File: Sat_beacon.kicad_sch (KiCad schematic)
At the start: 54 parts, among them IC1 LMX2581ESQE_NOPB, J1 Conn_01x03_Pin, J2 Conn_01x05_Pin, Q1 BC817, SW1 SW_Omron_B3FS, U1 STM32C011F6Px, U2 LD1117V33, U3 MCP1700x-330xxMB, Y1 FT2MHUPM10.0-T1

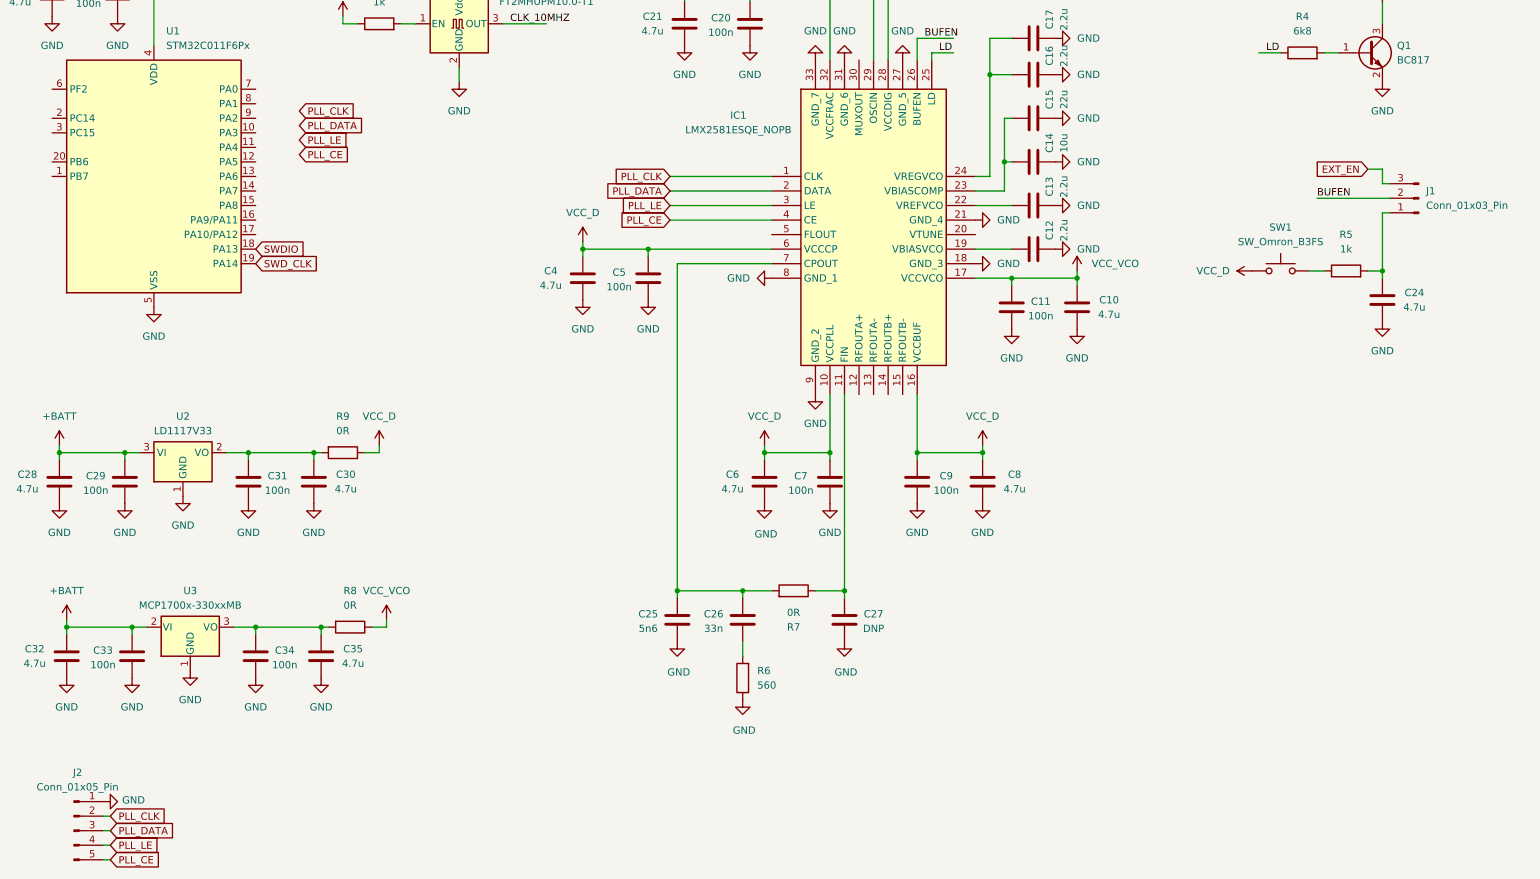
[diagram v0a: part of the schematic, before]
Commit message: added pin headers + signal nets fixes
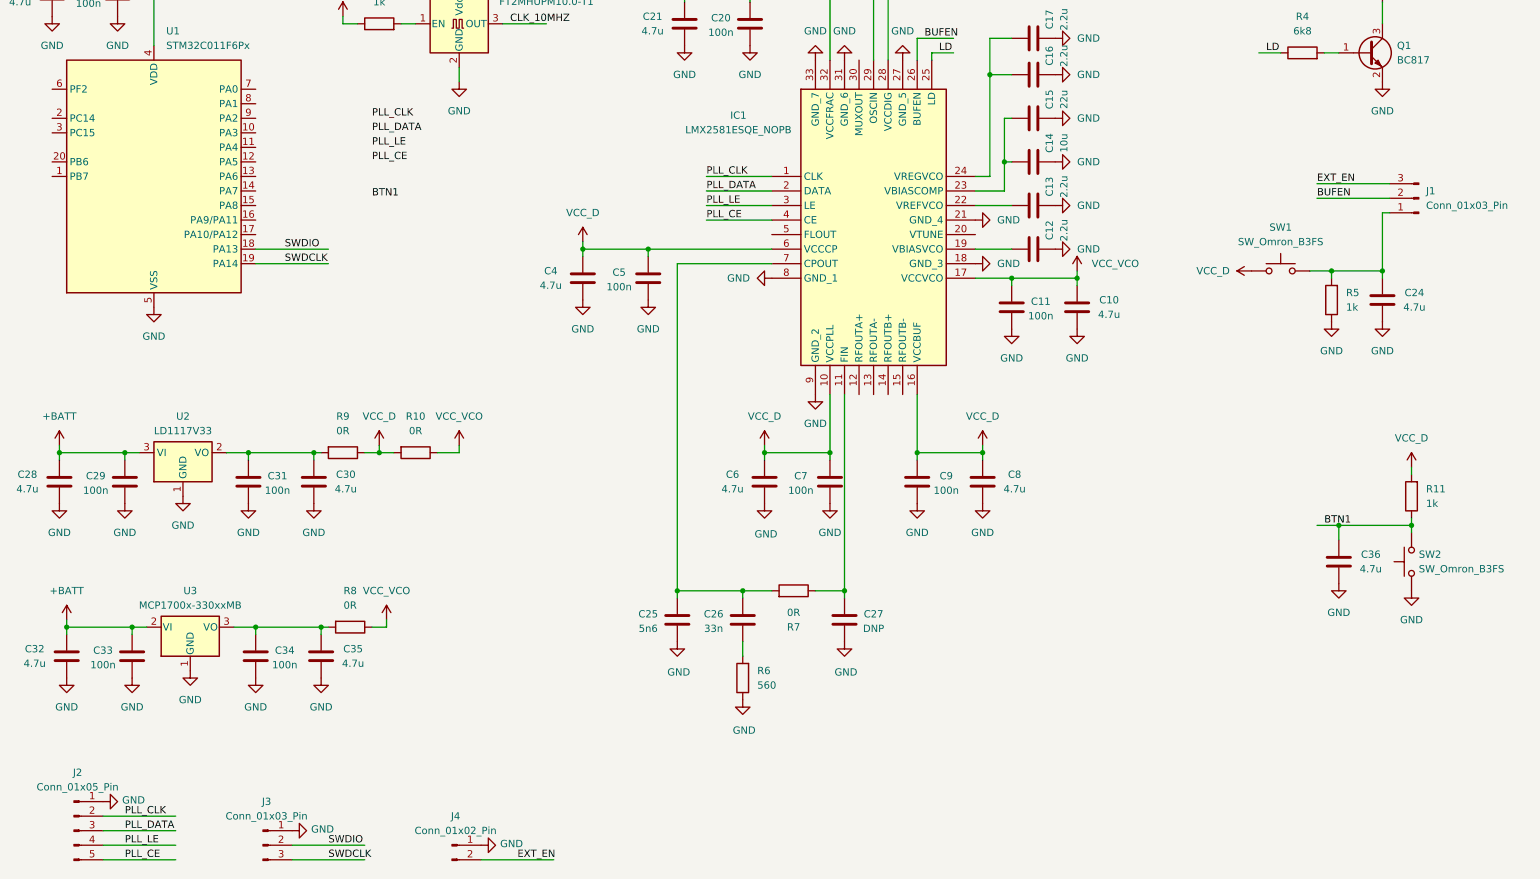
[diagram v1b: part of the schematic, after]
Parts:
- added C36: 4.7u, Capacitor_SMD:C_0805_2012Metric, symbol Device:C
- added J3: Conn_01x03_Pin, Connector_PinHeader_2.54mm:PinHeader_1x03_P2.54mm_Vertical, symbol Connector:Conn_01x03_Pin
- added J4: Conn_01x02_Pin, Connector_PinHeader_2.54mm:PinHeader_1x02_P2.54mm_Vertical, symbol Connector:Conn_01x02_Pin
- added R10: 0R, Resistor_SMD:R_0603_1608Metric, symbol Device:R
- added R11: 1k, Resistor_SMD:R_0603_1608Metric, symbol Device:R
- added SW2: SW_Omron_B3FS, Button_Switch_SMD:SW_SPST_Omron_B3FS-105xP, symbol Switch:SW_Omron_B3FS
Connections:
- net EXT_EN: now also J4.2 (Pin_2)
- net GND: now also R5.1, C36.1, J3.1 (Pin_1), J4.1 (Pin_1), SW2.1
- net SWDIO: now also J3.2 (Pin_2)
- net VCC_D: now also R10.2, R11.2
- net VCC_VCO: now also R10.1
- net at C24.2, J1.1 (Pin_1), R5.2: now also SW1.2
- net SWD_CLK renamed SWDCLK
- net SWDCLK: now also J3.3 (Pin_3)
- new net BTN1: C36.2, R11.1, SW2.2
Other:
- moved on the sheet: R5

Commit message: MCU-to-PLL pins added. Software folder created
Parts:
- added C37, C38, C39: 4.7u, Capacitor_SMD:C_0805_2012Metric, symbol Device:C
- added D2, D3: LED, LED_SMD:LED_0805_2012Metric, symbol Device:LED
- added Q2, Q3: BC817, Package_TO_SOT_SMD:SOT-23, symbol Transistor_BJT:BC817
- added R12, R13, R14: 1k, Resistor_SMD:R_0603_1608Metric, symbol Device:R
- added R15, R17: 330, Resistor_SMD:R_1206_3216Metric, symbol Device:R
- added R16, R18: 6k8, Resistor_SMD:R_0805_2012Metric, symbol Device:R
- added SW3, SW4, SW5: SW_Omron_B3FS, Button_Switch_SMD:SW_SPST_Omron_B3FS-105xP, symbol Switch:SW_Omron_B3FS
- D1: footprint LED_SMD:LED_1210_3225Metric -> LED_SMD:LED_0805_2012Metric
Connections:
- net GND: now also C37.1, C38.1, C39.1, Q2.2 (E), Q3.2 (E), SW3.1, SW4.1, SW5.1
- net PLL_CE: no longer IC1.4 (CE)
- net PLL_CLK: no longer IC1.1 (CLK)
- net PLL_DATA: no longer IC1.2 (DATA)
- net PLL_LE: no longer IC1.3 (LE)
- net VCC_D: now also D2.2 (A), D3.2 (A), R12.2, R13.2, R14.2
- net PLL_CE_1: now reaches U1.1 (PB7)
- net PLL_CE_1: now also IC1.4 (CE), U1.9 (PA2)
- net PLL_LED_1: now reaches U1.10 (PA3)
- net PLL_LED_2: now reaches U1.11 (PA4)
- net PLL_LED_2: now also R18.1
- net PLL_CE_2: now reaches U1.12 (PA5)
- net PLL_LE_2: now reaches U1.13 (PA6)
- net PLL_DATA_2: now reaches U1.14 (PA7)
- net PLL_CLK_2: now reaches U1.15 (PA8)
- net PLL_LE_1: now reaches U1.2 (PC14)
- net PLL_LE_1: now also IC1.3 (LE), U1.8 (PA1)
- net PLL_TOGGLE_2: now reaches U1.20 (PB6)
- net PLL_TOGGLE_2: now also C39.2, R14.1, SW5.2
- net PLL_DATA_1: now reaches U1.3 (PC15)
- net PLL_DATA_1: now also IC1.2 (DATA), U1.7 (PA0)
- net PLL_CLK_1: now reaches U1.6 (PF2)
- net PLL_CLK_1: now also IC1.1 (CLK)
- net BTN1 renamed PLL_BTN_1
- new net: D2.1 (K), R15.1
- new net: Q2.1 (B), R16.2
- new net: D3.1 (K), R17.1
- new net: Q3.3 (C), R17.2
- new net: Q3.1 (B), R18.2
- new net: Q2.3 (C), R15.2
- new net PLL_BTN_2: C37.2, R12.1, SW3.2
- new net PLL_TOGGLE_1: C38.2, R13.1, SW4.2
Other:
- moved on the sheet: C22, C23, C36, D1, Q1, R11, R3, R4, SW2, U1

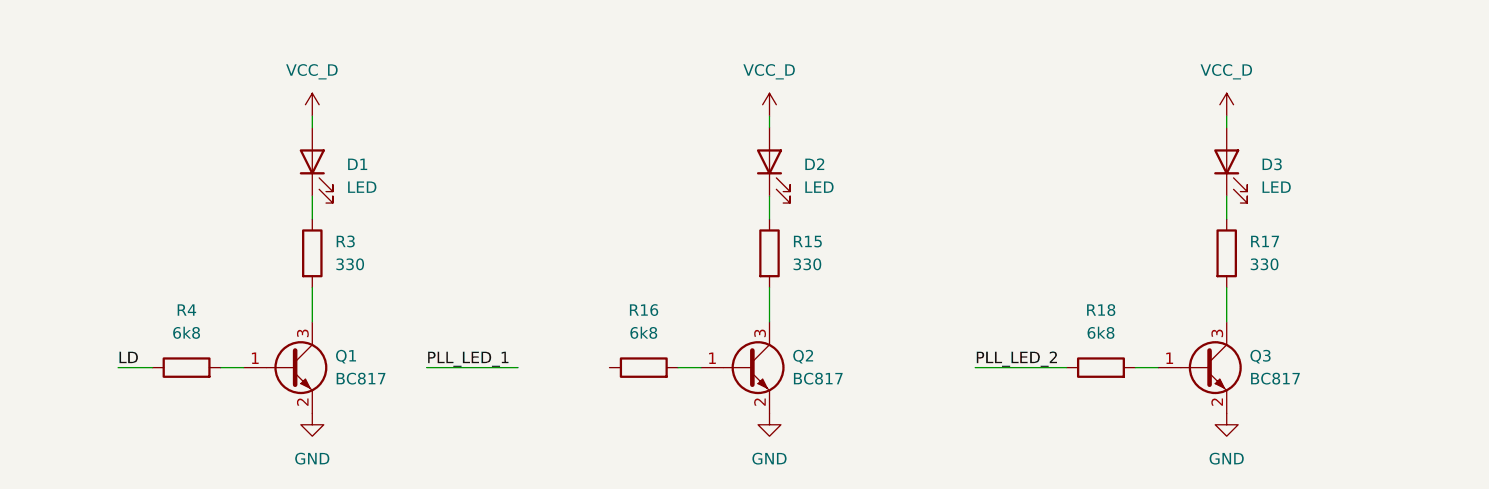
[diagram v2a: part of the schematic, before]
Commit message: picked LEDs and fixed resistors
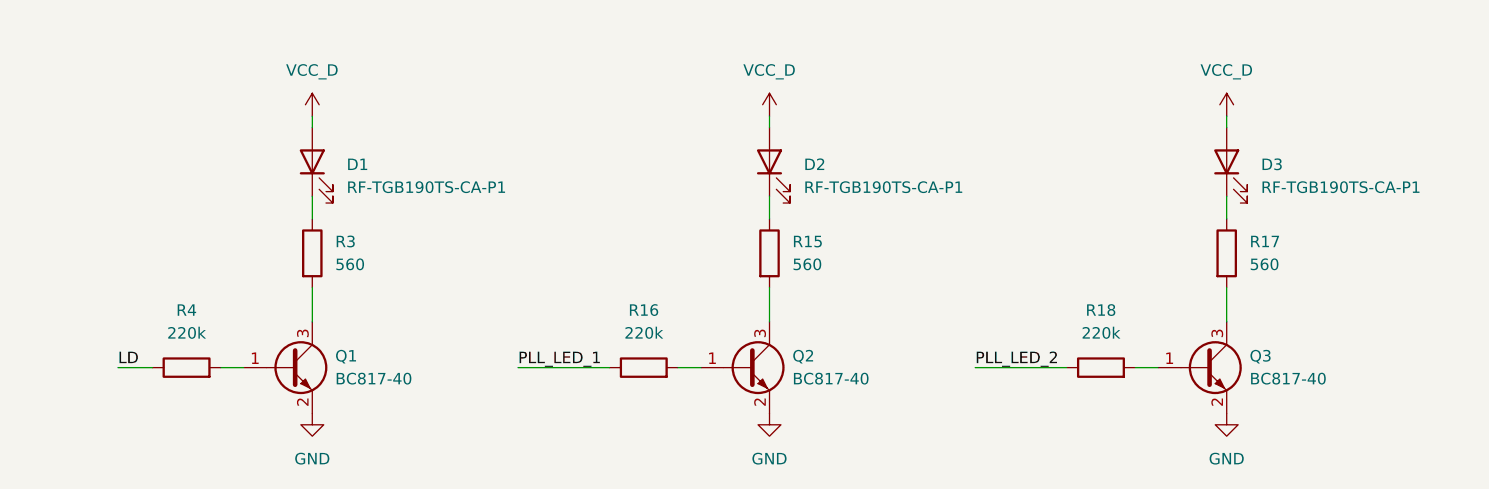
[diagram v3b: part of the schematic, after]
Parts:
- D1, D2, D3: value LED -> RF-TGB190TS-CA-P1; footprint LED_SMD:LED_0805_2012Metric -> LED_SMD:LED_0603_1608Metric
- Q1, Q2, Q3: value BC817 -> BC817-40
- R15, R17, R3: value 330 -> 560
- R16, R18, R4: value 6k8 -> 220k
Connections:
- net PLL_LED_1: now also R16.1
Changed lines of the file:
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@@
 	(wire
 		(pts
-			(xy 295.91 195.58) (xy 306.07 195.58)
+			(xy 306.07 195.58) (xy 316.23 195.58)
 		)
 		(stroke
@@
 	)
 	(label "PLL_LED_1"
-		(at 295.91 195.58 0)
+		(at 306.07 195.58 0)
 		(effects
 			(font
@@
 			)
 		)
-		(property "Value" "330"
+		(property "Value" "560"
 			(at 285.75 184.1499 0)
 			(effects
@@
 			)
 		)
-		(property "Value" "6k8"
+		(property "Value" "220k"
 			(at 269.24 191.77 90)
 			(effects
@@
 			)
 		)
-		(property "Value" "LED"
+		(property "Value" "RF-TGB190TS-CA-P1"
 			(at 337.82 175.5774 90)
 			(effects
@@
 			)
 		)
-		(property "Footprint" "LED_SMD:LED_0805_2012Metric"
+		(property "Footprint" "LED_SMD:LED_0603_1608Metric"
 			(at 334.01 172.72 0)
 			(effects
@@
 			)
 		)
-		(property "Value" "6k8"
+		(property "Value" "220k"
 			(at 320.04 191.77 90)
 			(effects
@@
 			)
 		)
-		(property "Value" "330"
+		(property "Value" "560"
 			(at 387.35 184.1499 0)
 			(effects
@@
 			)
 		)
-		(property "Value" "6k8"
+		(property "Value" "220k"
 			(at 370.84 191.77 90)
 			(effects
@@
 			)
 		)
-		(property "Value" "BC817"
+		(property "Value" "BC817-40"
 			(at 336.55 196.8499 0)
 			(effects
@@
 			)
 		)
-		(property "Value" "LED"
+		(property "Value" "RF-TGB190TS-CA-P1"
 			(at 287.02 175.5774 90)
 			(effects
@@
 			)
 		)
-		(property "Footprint" "LED_SMD:LED_0805_2012Metric"
+		(property "Footprint" "LED_SMD:LED_0603_1608Metric"
 			(at 283.21 172.72 0)
 			(effects
@@
 			)
 		)
-		(property "Value" "BC817"
+		(property "Value" "BC817-40"
 			(at 285.75 196.8499 0)
 			(effects
@@
 			)
 		)
-		(property "Value" "BC817"
+		(property "Value" "BC817-40"
 			(at 387.35 196.8499 0)
 			(effects
@@
 			)
 		)
-		(property "Value" "330"
+		(property "Value" "560"
 			(at 336.55 184.1499 0)
 			(effects
@@
 			)
 		)
-		(property "Value" "LED"
+		(property "Value" "RF-TGB190TS-CA-P1"
 			(at 388.62 175.5774 90)
 			(effects
@@
 			)
 		)
-		(property "Footprint" "LED_SMD:LED_0805_2012Metric"
+		(property "Footprint" "LED_SMD:LED_0603_1608Metric"
 			(at 384.81 172.72 0)
 			(effects

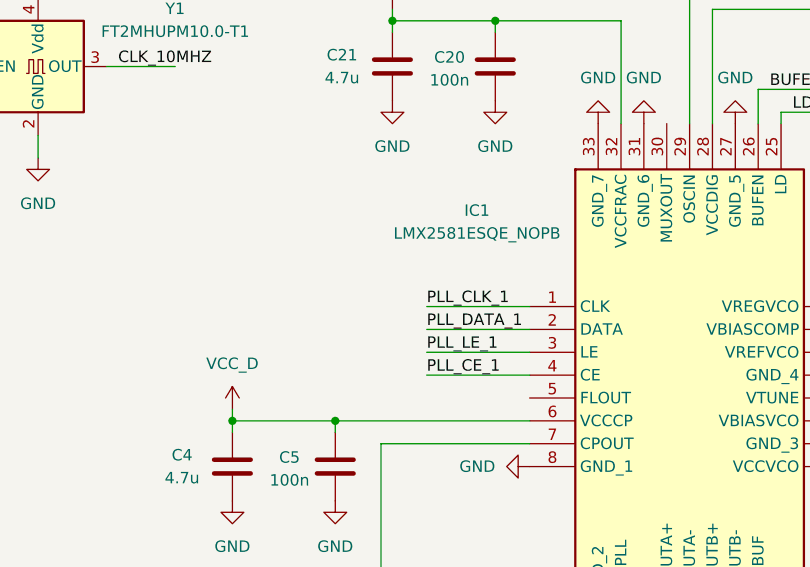
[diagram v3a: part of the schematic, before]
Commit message: PLL_LE pullup added
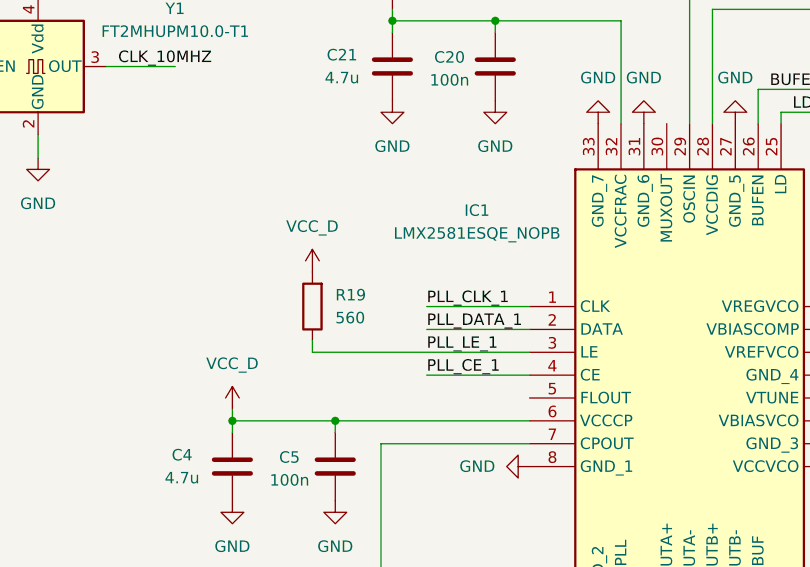
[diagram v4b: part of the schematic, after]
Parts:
- added R19: 560, Resistor_SMD:R_0603_1608Metric, symbol Device:R
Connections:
- net PLL_LE_1: now also R19.1
- net VCC_D: now also R19.2
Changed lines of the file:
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@@
 	(wire
 		(pts
-			(xy 139.7 77.47) (xy 151.13 77.47)
-		)
-		(stroke
-			(width 0)
-			(type default)
-		)
-	)
-	(wire
-		(pts
 			(xy 346.71 133.35) (xy 334.01 133.35)
 		)
@@
 	(wire
 		(pts
+			(xy 127 77.47) (xy 151.13 77.47)
+		)
+		(stroke
+			(width 0)
+			(type default)
+		)
+	)
+	(wire
+		(pts
 			(xy 86.36 45.72) (xy 88.9 45.72)
 		)
@@
 	(wire
 		(pts
+			(xy 127 76.2) (xy 127 77.47)
+		)
+		(stroke
+			(width 0)
+			(type default)
+		)
+	)
+	(wire
+		(pts
 			(xy 34.29 184.15) (xy 46.99 184.15)
 		)
@@
 	)
 	(symbol
+		(lib_id "Device:R")
+		(at 127 72.39 180)
+		(unit 1)
+		(exclude_from_sim no)
+		(in_bom yes)
+		(on_board yes)
+		(dnp no)
+		(fields_autoplaced yes)
+		(property "Reference" "R19"
+			(at 129.54 71.1199 0)
+			(effects
+				(font
+					(size 1.27 1.27)
+				)
+				(justify right)
+			)
+		)
+		(property "Value" "560"
+			(at 129.54 73.6599 0)
+			(effects
+				(font
+					(size 1.27 1.27)
+				)
+				(justify right)
+			)
+		)
+		(property "Footprint" "Resistor_SMD:R_0603_1608Metric"
+			(at 128.778 72.39 90)
+			(effects
+				(font
+					(size 1.27 1.27)
+				)
+				(hide yes)
+			)
+		)
+		(property "Datasheet" "~"
+			(at 127 72.39 0)
+			(effects
+				(font
+					(size 1.27 1.27)
+				)
+				(hide yes)
+			)
+		)
+		(property "Description" "Resistor"
+			(at 127 72.39 0)
+			(effects
+				(font
+					(size 1.27 1.27)
+				)
+				(hide yes)
+			)
+		)
+		(pin "1"
+		)
+		(pin "2"
+		)
+		(instances
+			(project "Sat_beacon"
+				(path "/d50b57a8-fbd1-4b9f-a519-640b54fbccac"
+					(reference "R19")
+					(unit 1)
+				)
+			)
+		)
+	)
+	(symbol
 		(lib_id "Device:C")
 		(at 149.86 125.73 180)
@@
 					(unit 1)
 				)
+			)
+		)
+	)
+	(symbol
+		(lib_id "power:VCC")
+		(at 127 68.58 0)
+		(mirror y)
+		(unit 1)
+		(exclude_from_sim no)
+		(in_bom yes)
+		(on_board yes)
+		(dnp no)
+		(fields_autoplaced yes)
+		(property "Reference" "#PWR084"
+			(at 127 72.39 0)
+			(effects
+				(font
+					(size 1.27 1.27)
+				)
+				(hide yes)
+			)
+		)
+		(property "Value" "VCC_D"
+			(at 127 63.5 0)
+			(effects
+				(font
+					(size 1.27 1.27)
+				)
+			)
+		)
+		(property "Footprint" ""
+			(at 127 68.58 0)
+			(effects
+				(font
+					(size 1.27 1.27)
+				)
+				(hide yes)
+			)
+		)
+		(property "Datasheet" ""
+			(at 127 68.58 0)
+			(effects
+				(font
+					(size 1.27 1.27)
+				)
+				(hide yes)
+			)
+		)
+		(property "Description" "Power symbol creates a global label with name \"VCC\""
+			(at 127 68.58 0)
+			(effects
+				(font
+					(size 1.27 1.27)
+				)
+				(hide yes)
+			)
+		)
+		(pin "1"
+		)
+		(instances
+			(project "Sat_beacon"
+				(path "/d50b57a8-fbd1-4b9f-a519-640b54fbccac"
+					(reference "#PWR084")
+					(unit 1)
+				)

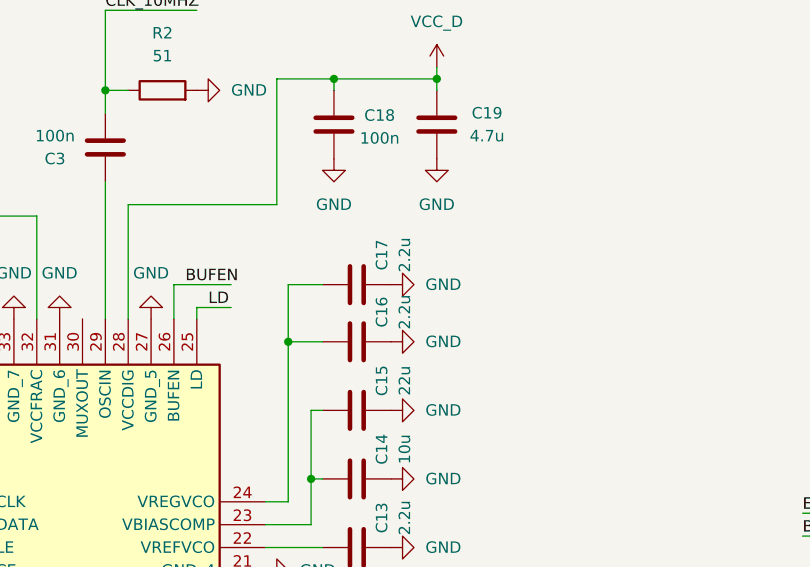
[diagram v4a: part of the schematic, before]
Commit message: fixed PLL caps
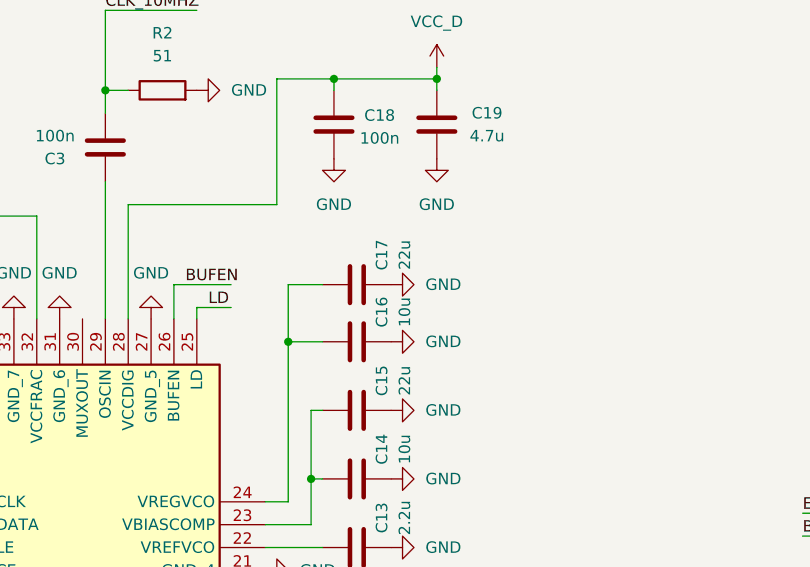
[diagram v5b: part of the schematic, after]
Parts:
- C16: value 2.2u -> 10u
- C17: value 2.2u -> 22u
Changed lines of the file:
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@@
 			)
 		)
-		(property "Value" "2.2u"
+		(property "Value" "10u"
 			(at 202.184 51.308 0)
 			(effects
@@
 			)
 		)
-		(property "Value" "2.2u"
+		(property "Value" "22u"
 			(at 202.184 44.958 0)
 			(effects
